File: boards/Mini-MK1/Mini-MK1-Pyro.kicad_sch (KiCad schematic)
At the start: 0 parts

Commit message: Added Under voltage Supervisor Symbol
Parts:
- added U2: PTPS3842A011DRLRQ1, SOT-5X3-6_DRL_TEX, symbol Power_Supervisor:PTPS3842A011DRLRQ1
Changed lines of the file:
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@@
 	(generator_version "9.0")
 	(paper "A4")
+	(symbol
+		(lib_name "PTPS3842A011DRLRQ1_1")
+		(lib_id "Power_Supervisor:PTPS3842A011DRLRQ1")
+		(at 24.13 54.61 0)
+		(unit 1)
+		(exclude_from_sim no)
+		(in_bom yes)
+		(on_board yes)
+		(dnp no)
+		(fields_autoplaced yes)
+		(property "Reference" "U2"
+			(at 44.45 44.45 0)
+			(effects
+				(font
+					(size 1.524 1.524)
+				)
+			)
+		)
+		(property "Value" "PTPS3842A011DRLRQ1"
+			(at 44.45 46.99 0)
+			(effects
+				(font
+					(size 1.524 1.524)
+				)
+			)
+		)
+		(property "Footprint" "SOT-5X3-6_DRL_TEX"
+			(at 24.13 54.61 0)
+			(effects
+				(font
+					(size 1.27 1.27)
+					(italic yes)
+				)
+				(hide yes)
+			)
+		)
+		(property "Datasheet" "https://www.ti.com/lit/gpn/tps3842-q1"
+			(at 24.13 54.61 0)
+			(effects
+				(font
+					(size 1.27 1.27)
+					(italic yes)
+				)
+				(hide yes)
+			)
+		)
+		(property "Description" ""
+			(at 24.13 54.61 0)
+			(effects
+				(font
+					(size 1.27 1.27)
+				)
+				(hide yes)
+			)
+		)
+		(pin "1"
+		)
+		(pin "2"
+		)
+		(pin "3"
+		)
+		(pin "6"
+		)
+		(pin "5"
+		)
+		(pin "4"
+		)
+		(instances
+			(project ""
+				(path "/0941d445-abe5-4c4a-84ea-6134de0a1f2b/1e5adeaa-def4-48f2-a5f7-5a3c1ef3978e"
+					(reference "U2")
+					(unit 1)
+				)
+			)
+		)
+	)
 )

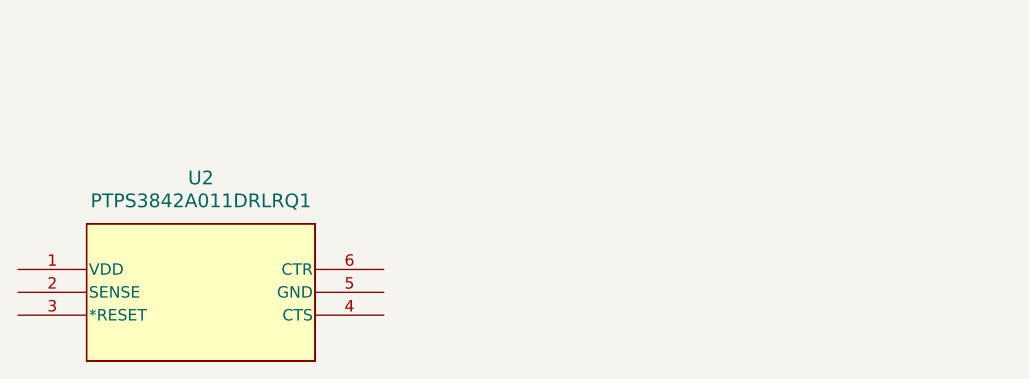
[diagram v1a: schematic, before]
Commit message: Smaller Expander for Pyro
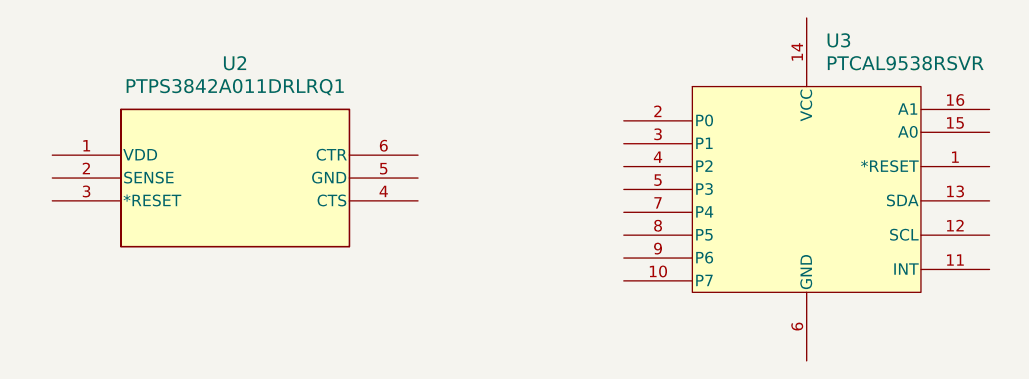
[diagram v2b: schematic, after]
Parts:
- added U3: PTCAL9538RSVR, UQFN16_RSV_TEX, symbol Interface_Expander_Texas:PTCAL9538RSVR
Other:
- moved on the sheet: U2
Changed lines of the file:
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@@
 	(paper "A4")
+	(symbol
+		(lib_name "PTCAL9538RSVR_1")
+		(lib_id "Interface_Expander_Texas:PTCAL9538RSVR")
+		(at 91.44 36.83 0)
+		(unit 1)
+		(exclude_from_sim no)
+		(in_bom yes)
+		(on_board yes)
+		(dnp no)
+		(fields_autoplaced yes)
+		(property "Reference" "U3"
+			(at 113.9033 29.21 0)
+			(effects
+				(font
+					(size 1.524 1.524)
+				)
+				(justify left)
+			)
+		)
+		(property "Value" "PTCAL9538RSVR"
+			(at 113.9033 31.75 0)
+			(effects
+				(font
+					(size 1.524 1.524)
+				)
+				(justify left)
+			)
+		)
+		(property "Footprint" "UQFN16_RSV_TEX"
+			(at 137.16 22.86 0)
+			(effects
+				(font
+					(size 1.27 1.27)
+					(italic yes)
+				)
+				(hide yes)
+			)
+		)
+		(property "Datasheet" "https://www.ti.com/lit/gpn/tcal9538"
+			(at 136.906 19.558 0)
+			(effects
+				(font
+					(size 1.27 1.27)
+					(italic yes)
+				)
+				(hide yes)
+			)
+		)
+		(property "Description" ""
+			(at 91.44 36.83 0)
+			(effects
+				(font
+					(size 1.27 1.27)
+				)
+				(hide yes)
+			)
+		)
+		(pin "16"
+		)
+		(pin "15"
+		)
+		(pin "1"
+		)
+		(pin "13"
+		)
+		(pin "12"
+		)
+		(pin "11"
+		)
+		(pin "2"
+		)
+		(pin "3"
+		)
+		(pin "4"
+		)
+		(pin "5"
+		)
+		(pin "7"
+		)
+		(pin "8"
+		)
+		(pin "9"
+		)
+		(pin "10"
+		)
+		(pin "14"
+		)
+		(pin "6"
+		)
+		(instances
+			(project ""
+				(path "/0941d445-abe5-4c4a-84ea-6134de0a1f2b/1e5adeaa-def4-48f2-a5f7-5a3c1ef3978e"
+					(reference "U3")
+					(unit 1)
+				)
+			)
+		)
+	)
 	(symbol
 		(lib_name "PTPS3842A011DRLRQ1_1")
 		(lib_id "Power_Supervisor:PTPS3842A011DRLRQ1")
-		(at 24.13 54.61 0)
+		(at 27.94 41.91 0)
 		(unit 1)
 		(exclude_from_sim no)
@@
 		(fields_autoplaced yes)
 		(property "Reference" "U2"
-			(at 44.45 44.45 0)
+			(at 48.26 31.75 0)
 			(effects
 				(font
@@
 		)
 		(property "Value" "PTPS3842A011DRLRQ1"
-			(at 44.45 46.99 0)
+			(at 48.26 34.29 0)
 			(effects
 				(font
@@
 		)
 		(property "Footprint" "SOT-5X3-6_DRL_TEX"
-			(at 24.13 54.61 0)
+			(at 27.94 41.91 0)
 			(effects
 				(font
@@
 		)
 		(property "Datasheet" "https://www.ti.com/lit/gpn/tps3842-q1"
-			(at 24.13 54.61 0)
+			(at 27.94 41.91 0)
 			(effects
 				(font
@@
 		)
 		(property "Description" ""
-			(at 24.13 54.61 0)
+			(at 27.94 41.91 0)
 			(effects
 				(font

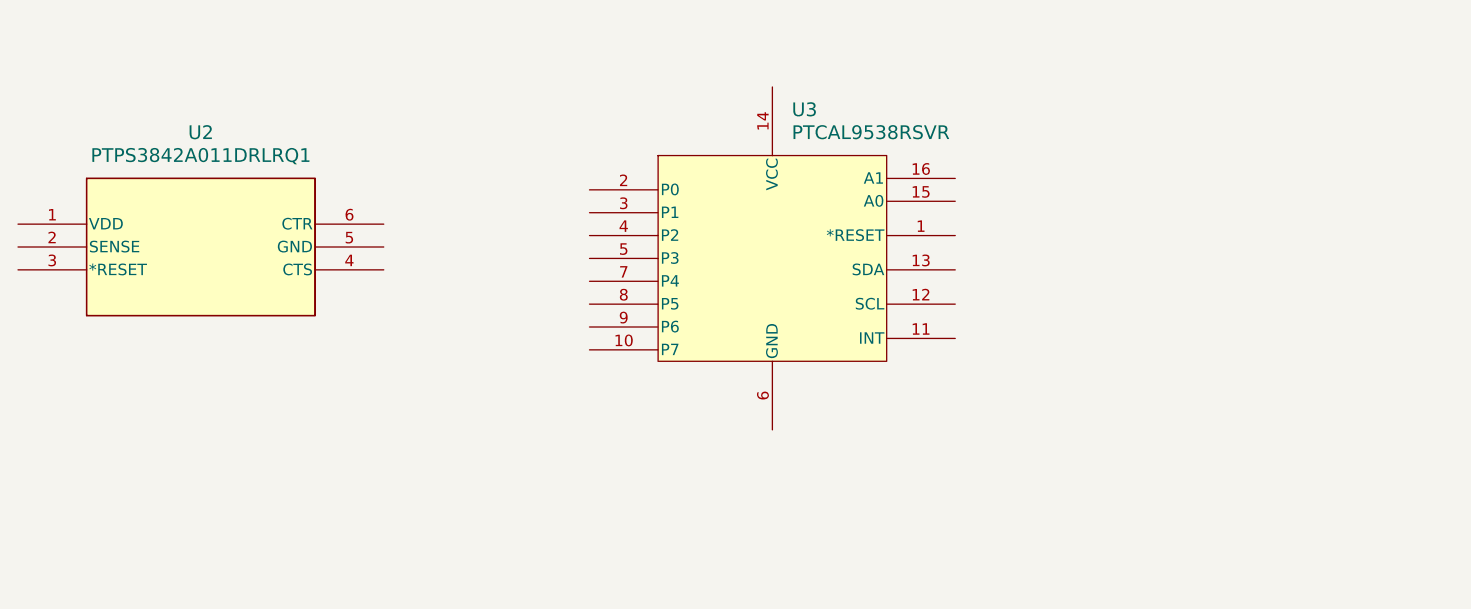
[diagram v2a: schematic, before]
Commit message: Added schematic for GPIO expander
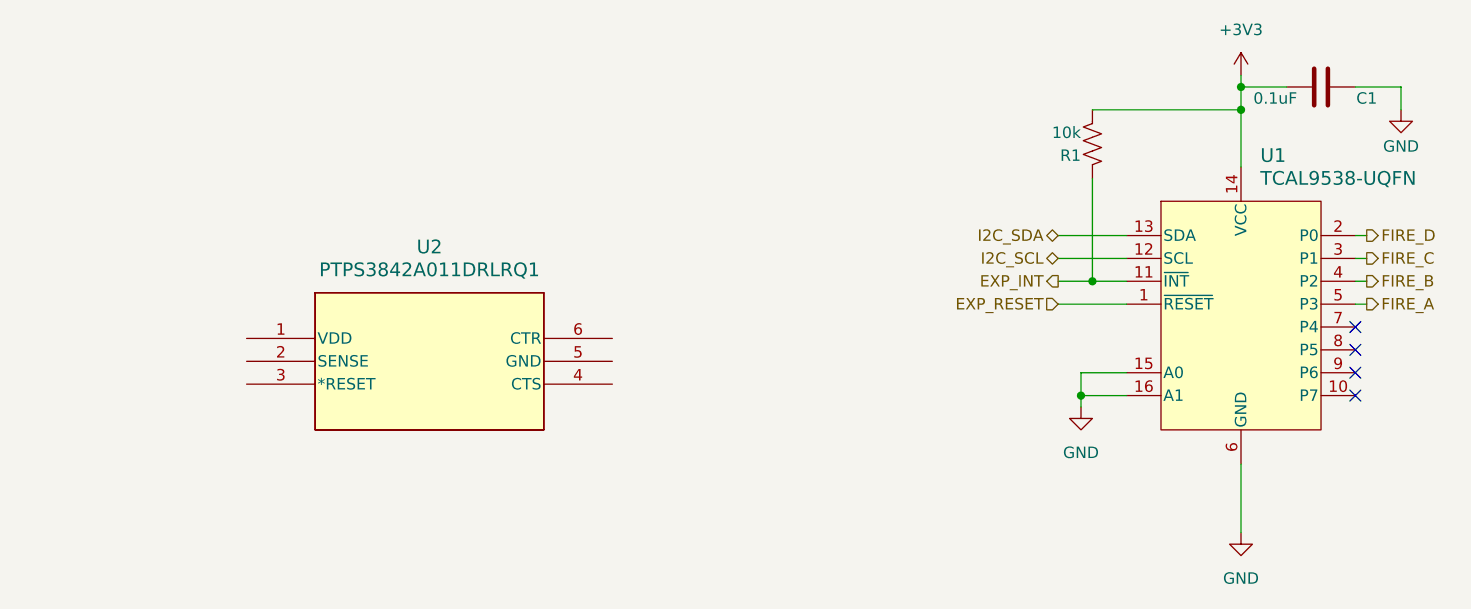
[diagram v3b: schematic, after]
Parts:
- removed U3: PTCAL9538RSVR, UQFN16_RSV_TEX, symbol Interface_Expander_Texas:PTCAL9538RSVR
- added C1: 0.1uF, Capacitor_SMD:C_0603_1608Metric, symbol Device:C
- added R1: 10k, Resistor_SMD:R_0603_1608Metric, symbol Device:R_US
- added U1: TCAL9538-UQFN, UQFN16_RSV_TEX, symbol Interface_Expander_Texas:PTCAL9538RSVR
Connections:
- new net +3V3: C1.2, R1.2, U1.14 (VCC)
- new net EXP_INT: R1.1, U1.11 (~{INT})
- new net EXP_RESET: U1.1 (~{RESET})
- new net FIRE_A: U1.5 (P3)
- new net FIRE_B: U1.4 (P2)
- new net FIRE_C: U1.3 (P1)
- new net FIRE_D: U1.2 (P0)
- new net GND: C1.1, U1.15 (A0), U1.16 (A1), U1.6 (GND)
- new net I2C_SCL: U1.12 (SCL)
- new net I2C_SDA: U1.13 (SDA)
- no-connect marks 0 -> 4
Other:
- moved on the sheet: U2

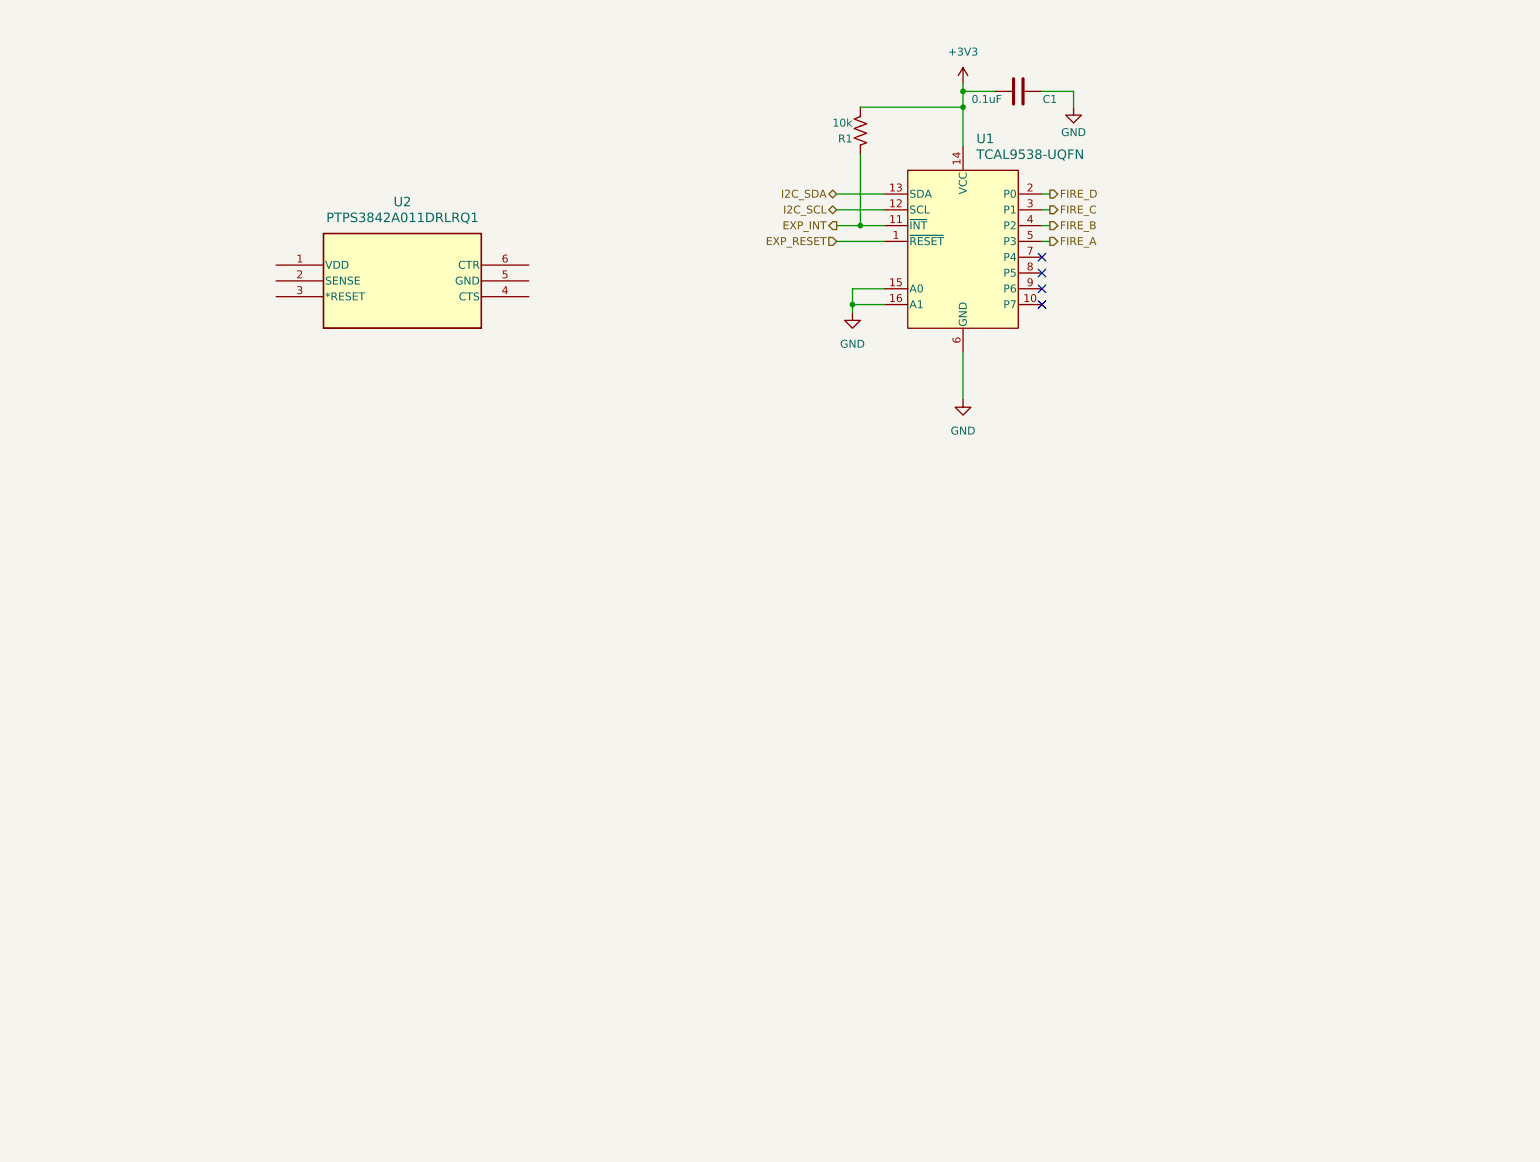
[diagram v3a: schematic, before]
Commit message: Added MAX symbol, Copied Pyro channels, Added labels and current limit switch
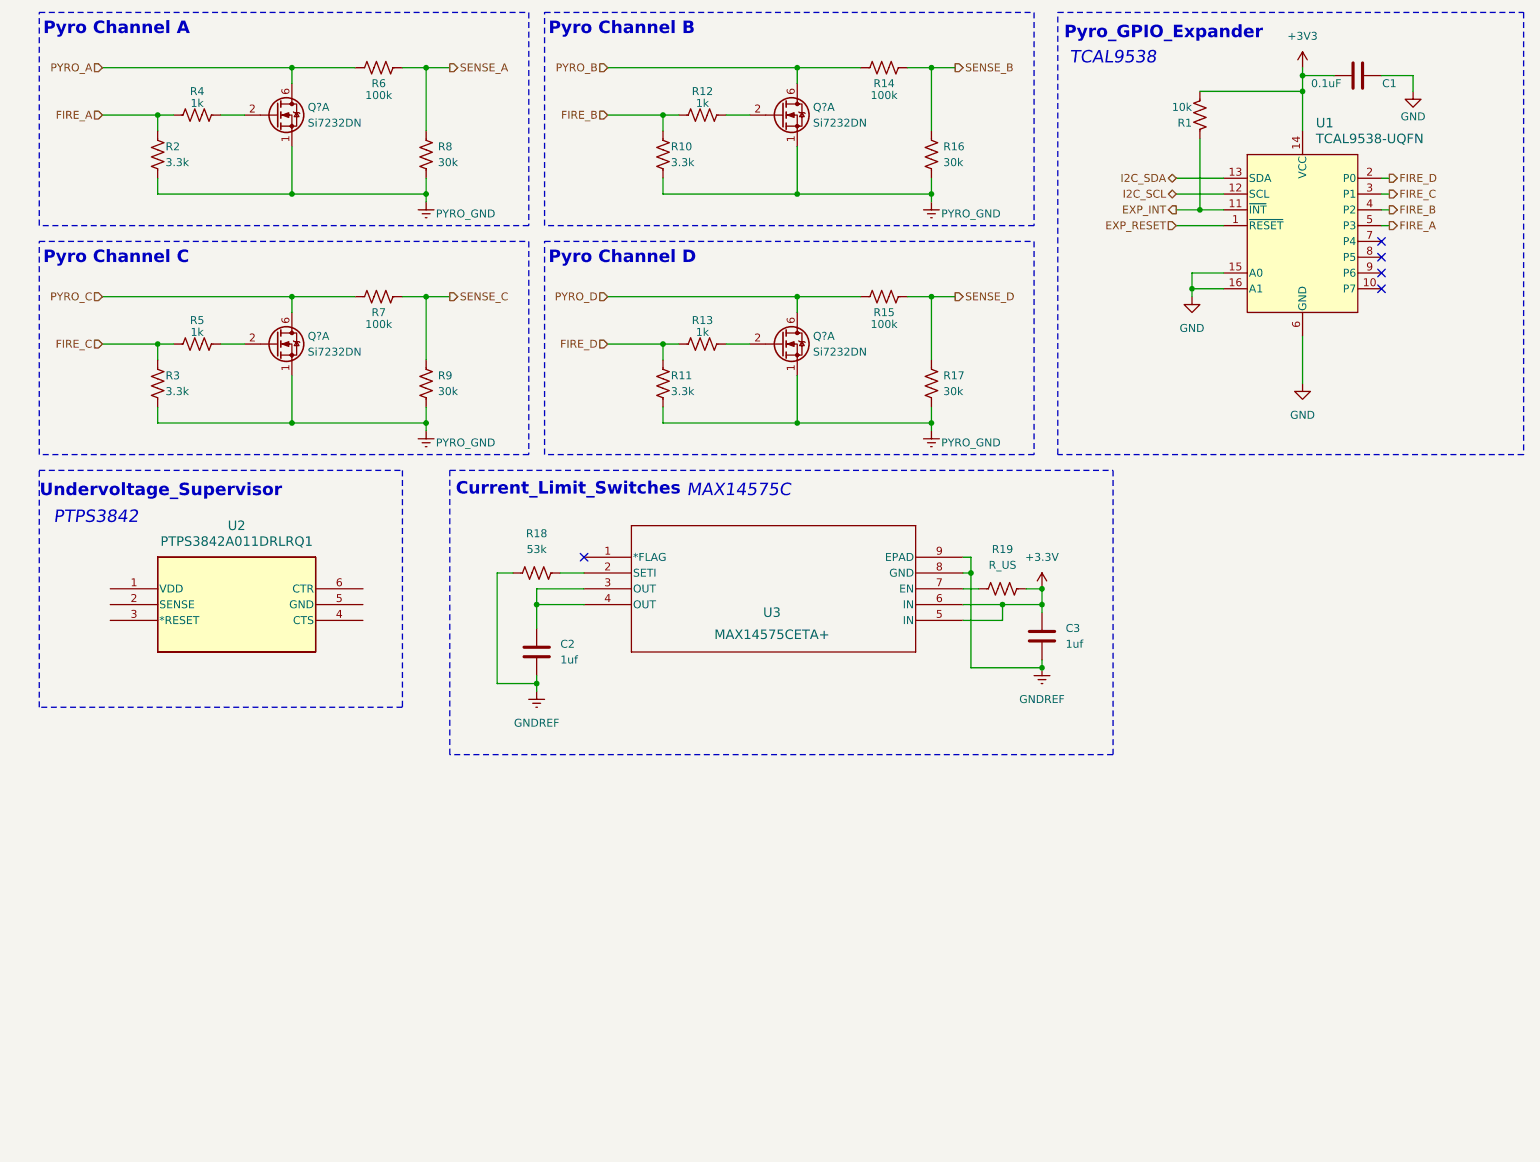
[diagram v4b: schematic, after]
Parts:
- added C2, C3: 1uf, symbol Device:C
- added Q? (x4): Si7232DN, Transistor_FET_Vishay:Vishay_PowerPAK_1212-8_Dual, symbol Transistor_FET_Vishay:Si7232DN
- added R10, R11, R2, R3: 3.3k, Resistor_SMD:R_0603_1608Metric, symbol Device:R_US
- added R12, R13, R4, R5: 1k, Resistor_SMD:R_0603_1608Metric, symbol Device:R_US
- added R14, R15, R6, R7: 100k, Resistor_SMD:R_0603_1608Metric, symbol Device:R_US
- added R16, R17, R8, R9: 30k, Resistor_SMD:R_0603_1608Metric, symbol Device:R_US
- added R18: 53k, symbol Device:R_US
- added R19: R_US, symbol Device:R_US
- added U3: MAX14575CETA+, 21-0168E_T822-2_MXM, symbol Current_Limit_Switch:MAX14575CETA+
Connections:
- net FIRE_A: now also R2.1, R4.1
- net FIRE_B: now also R10.1, R12.1
- net FIRE_C: now also R3.1, R5.1
- net FIRE_D: now also R11.1, R13.1
- new net: Q?.2 (G1), R12.2
- new net: Q?.2 (G1), R13.2
- new net: R18.2, U3.2 (SETI)
- new net: C2.1, U3.3 (OUT), U3.4 (OUT)
- new net: Q?.2 (G1), R5.2
- new net: Q?.2 (G1), R4.2
- new net: R19.1, U3.7 (EN)
- new net +3.3V: C3.1, R19.2, U3.5 (IN), U3.6 (IN)
- new net GNDREF: C2.2, C3.2, R18.1, U3.8 (GND), U3.9 (EPAD)
- new net PYRO_A: Q?.6 (D1), R6.2
- new net PYRO_B: Q?.6 (D1), R14.2
- new net PYRO_C: Q?.6 (D1), R7.2
- new net PYRO_D: Q?.6 (D1), R15.2
- new net PYRO_GND: Q?.1 (S1), Q?.1 (S1), Q?.1 (S1), Q?.1 (S1), R10.2, R11.2, R16.1, R17.1, R2.2, R3.2, R8.1, R9.1
- new net SENSE_A: R6.1, R8.2
- new net SENSE_B: R14.1, R16.2
- new net SENSE_C: R7.1, R9.2
- new net SENSE_D: R15.1, R17.2
- no-connect marks 4 -> 5
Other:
- note added: "Current_Limit_Switches"
- note added: "MAX14575C"
- note added: "PTPS3842"
- note added: "Pyro Channel A"
- note added: "Pyro Channel B"
- note added: "Pyro Channel C"
- note added: "Pyro Channel D"
- note added: "Pyro_GPIO_Expander"
- note added: "TCAL9538"
- note added: "Undervoltage_Supervisor"
- moved on the sheet: C1, R1, U1, U2
